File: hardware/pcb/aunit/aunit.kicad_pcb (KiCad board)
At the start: 2 copper layers, 62.2 x 21.6 mm, 48 parts, among them J1 BUS, J2 Input A, J3 Input B, J4 Control, J5 Flags, J6 Power, U1 74HC283, U2 74HC283, U3 74HC86, U4 74HC86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

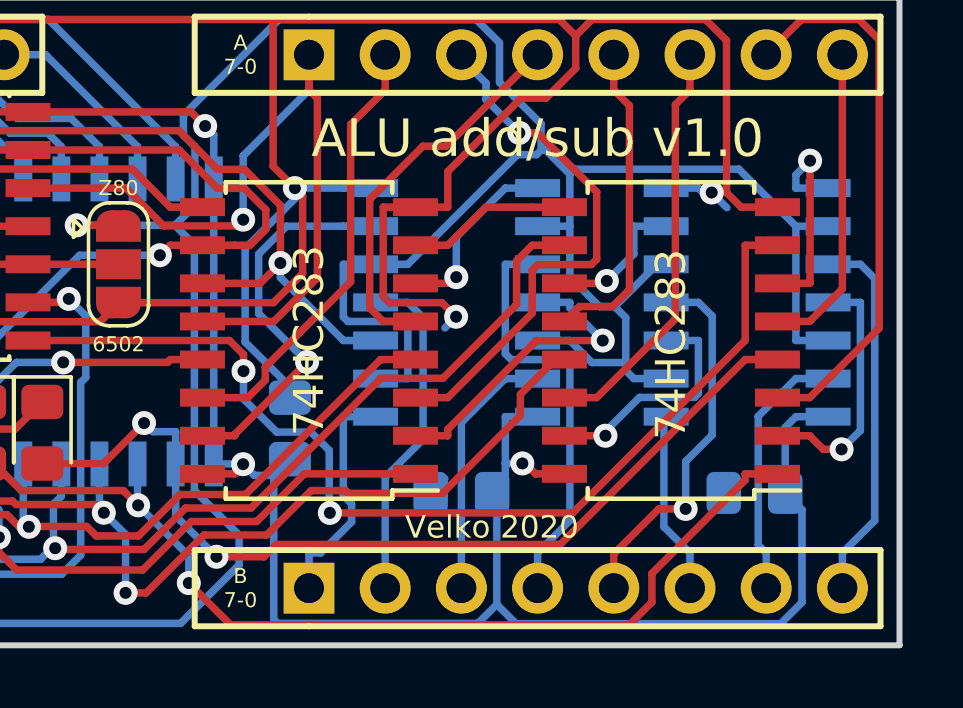
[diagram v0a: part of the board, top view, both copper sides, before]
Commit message: Corrected adder footprints on AUnit, needs re-routing
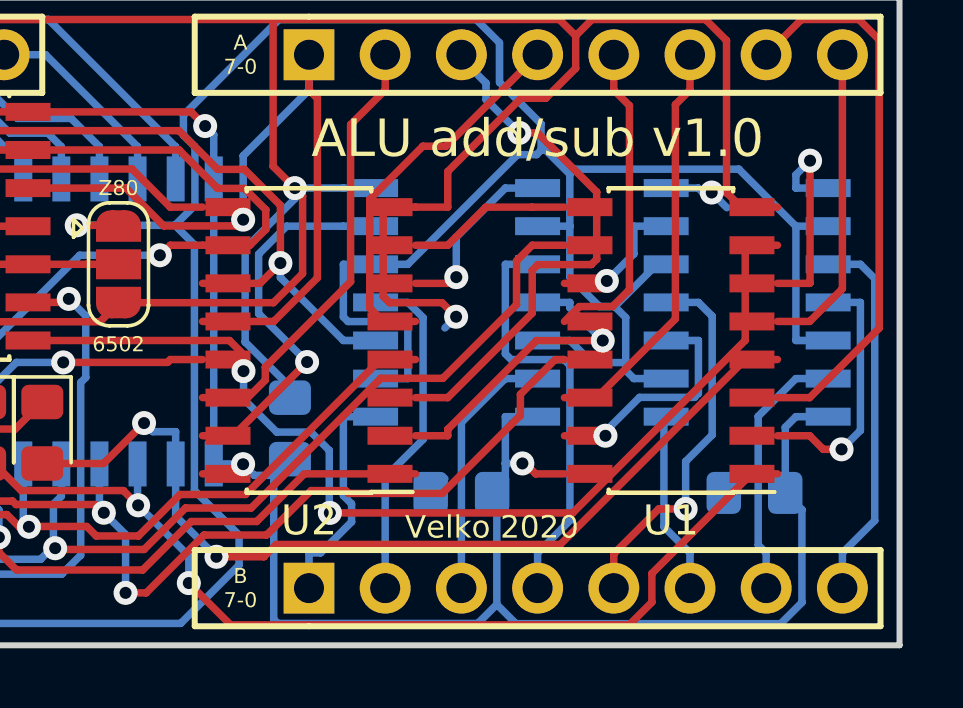
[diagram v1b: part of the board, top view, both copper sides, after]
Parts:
- U1, U2: footprint Package_SO:SOIC-16W_5.3x10.2mm_P1.27mm -> Package_SO:SOIC-16_3.9x9.9mm_P1.27mm

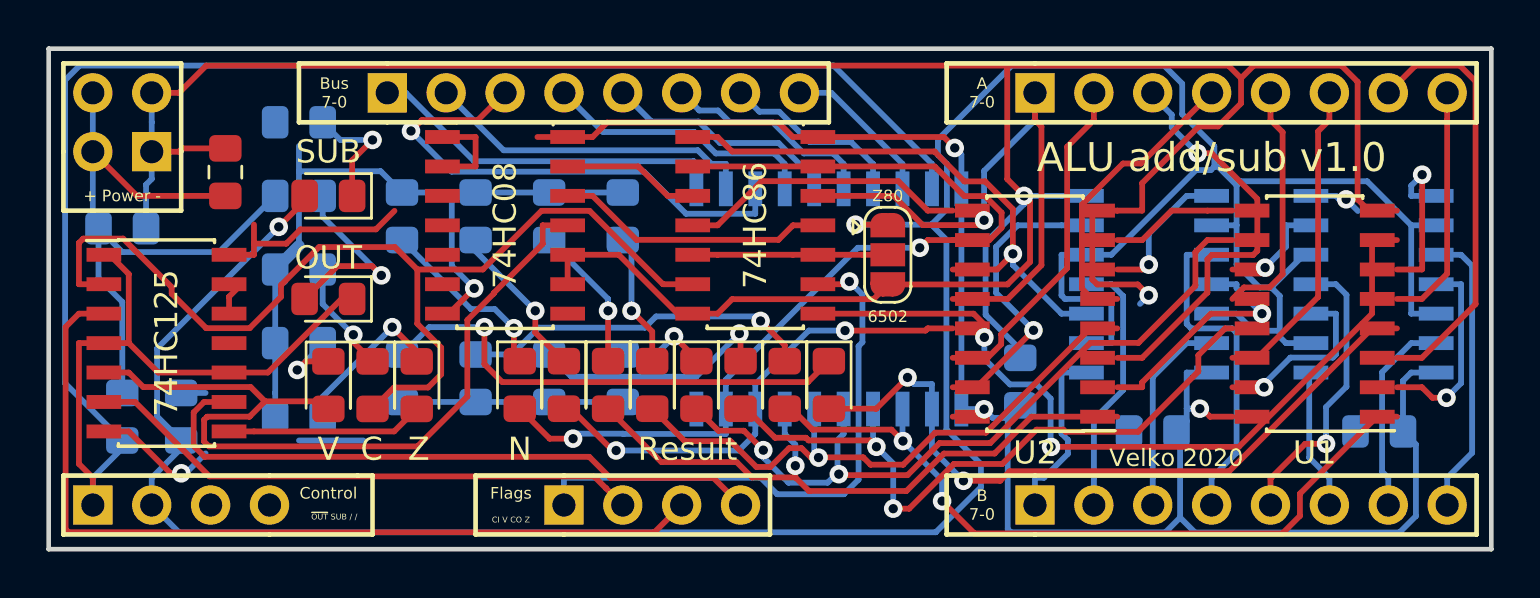
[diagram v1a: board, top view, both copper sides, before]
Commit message: Rerouted for new footprints (checkpoint)
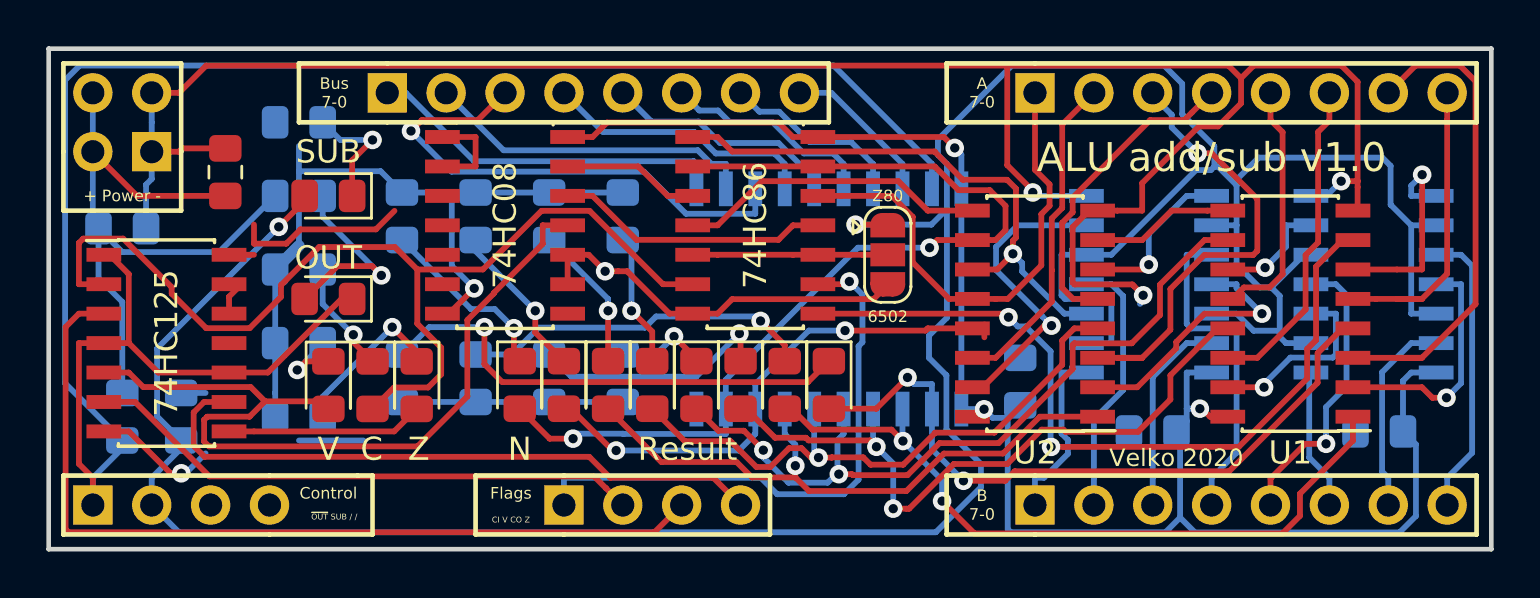
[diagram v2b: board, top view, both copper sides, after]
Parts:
- moved U1 1.05 mm to (88.5, 47.6)
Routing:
- net GND: track 184.0 -> 165.3 mm, vias 5 -> 6
- net A7: track 26.2 -> 21.1 mm, vias 1 -> 0
- net ADD_SUB: track 137.7 -> 140.7 mm
- net A1: track 18.5 -> 21.5 mm
- net A0: track 10.4 -> 13.4 mm
- net VCC: track 119.8 -> 117.0 mm
- net A5: track 17.8 -> 19.9 mm
- net /B1I: track 8.56 -> 10.5 mm
- net /B0I: track 7.36 -> 9.25 mm
- net SUM1: track 33.3 -> 31.9 mm
- net SUM6: track 21.0 -> 22.2 mm
- net SUM0: track 31.3 -> 30.1 mm
- net SUM7: track 41.3 -> 42.4 mm
- net SUM5: track 27.9 -> 26.8 mm
- net /B4I: track 6.17 -> 7.09 mm
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
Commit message: Power and ground plane optimizations
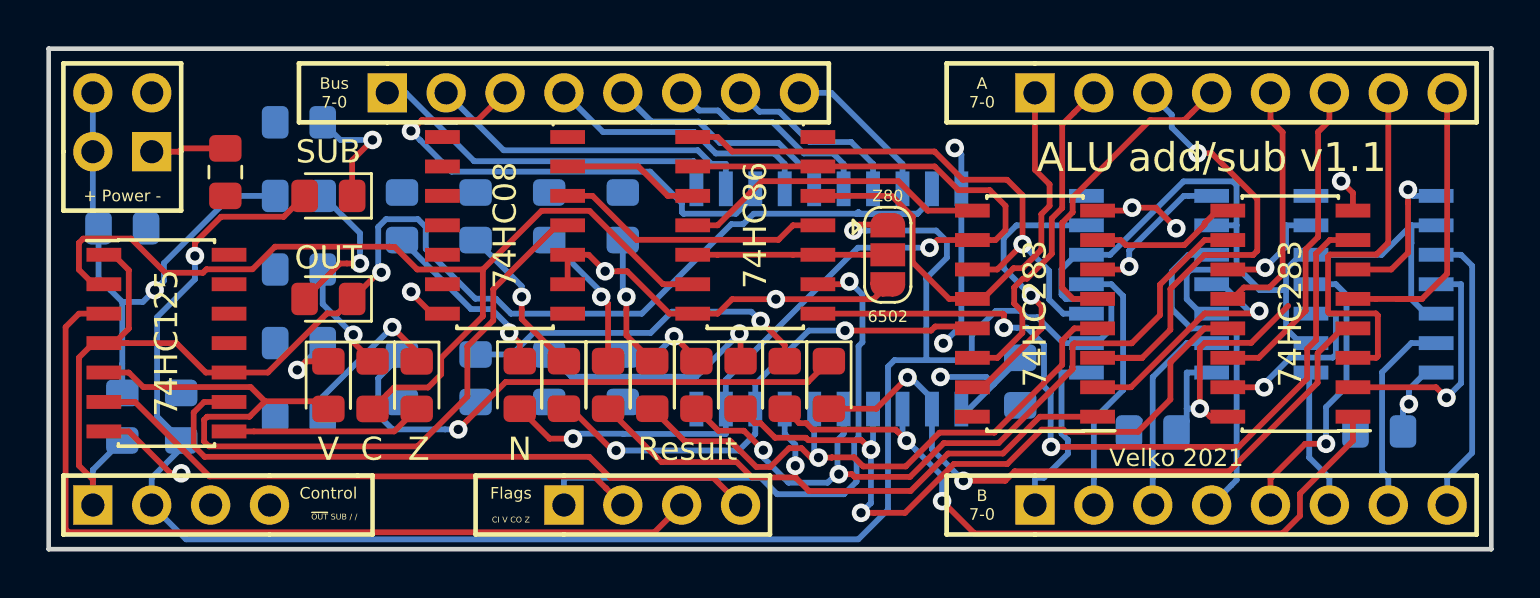
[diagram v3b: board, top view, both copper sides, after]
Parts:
- turned C2 to 270 degrees
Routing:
- net GND: track 165.3 -> 32.3 mm, vias 6 -> 7
- net VCC: track 117.0 -> 55.1 mm, vias 3 -> 6
- net ~OUT~: track 85.6 -> 64.2 mm, vias 0 -> 1
- net ADD_SUB: track 140.7 -> 123.7 mm
- net A1: track 21.5 -> 16.8 mm
- net Net-(D0-Pad1): track 21.2 -> 24.0 mm
- net /B0I: track 9.25 -> 6.76 mm
- net CARRYD: track 44.2 -> 41.7 mm
- net Net-(D8-Pad2): track 8.54 -> 6.60 mm
- net SUM2: track 30.1 -> 31.7 mm
- net /B6I: track 13.2 -> 12.4 mm
- net /CII: track 34.2 -> 34.8 mm
- net B7I: track 24.2 -> 24.7 mm
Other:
- board text added: "ALU add/sub v1.1"
- board text added: "Velko 2021"
- board text removed: "ALU add/sub v1.0"
- board text removed: "Velko 2020"

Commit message: Remove all tracks
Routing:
- net ADD_SUB: track 123.7 -> 0.00 mm, vias 2 -> 0
- net ~OUT~: track 64.2 -> 0.00 mm, vias 1 -> 0
- net VCC: track 55.1 -> 0.00 mm, vias 6 -> 0
- net SUM7: track 42.4 -> 0.00 mm, vias 2 -> 0
- net CARRYD: track 41.7 -> 0.00 mm
- net COUT: track 37.7 -> 0.00 mm
- net OVFD: track 36.0 -> 0.00 mm
- net /CII: track 34.8 -> 0.00 mm, vias 2 -> 0
- net SUM3: track 33.3 -> 0.00 mm, vias 2 -> 0
- net GND: track 32.3 -> 0.00 mm, vias 7 -> 0
- net SUM1: track 32.1 -> 0.00 mm, vias 2 -> 0
- net SUM2: track 31.7 -> 0.00 mm, vias 2 -> 0
- net SUM0: track 29.8 -> 0.00 mm, vias 2 -> 0
- net ZIN: track 27.8 -> 0.00 mm
- net SUM5: track 26.8 -> 0.00 mm, vias 1 -> 0
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- removed copper zone on B.Cu, net GND
- removed copper zone on F.Cu, net VCC

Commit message: Move stuff around
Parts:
- added C6: 100nF, Capacitor_SMD:C_0805_2012Metric_Pad1.15x1.40mm_HandSolder, F.Cu at (59.3, 41.3)
- added C7: 100nF, Capacitor_SMD:C_0805_2012Metric_Pad1.15x1.40mm_HandSolder, F.Cu at (79.2, 53.3)
- added C8: 100nF, Capacitor_SMD:C_0805_2012Metric_Pad1.15x1.40mm_HandSolder, F.Cu at (71.0, 40.4)
- added C9: 100nF, Capacitor_SMD:C_0805_2012Metric_Pad1.15x1.40mm_HandSolder, F.Cu at (90.4, 53.2)
- moved R4 3.81 mm to (56.3, 45.1)
- moved U2 3.72 mm to (81.2, 47.1)
- moved U1 3.50 mm to (91.9, 47.1)
- moved R3 3.43 mm to (56.3, 50.4)
- moved R5 2.82 mm to (54.2, 45.1)
- moved C2 2.80 mm to (74.0, 50.7), turned to 90 degrees
- moved U7 2.29 mm to (66.3, 46.9)
- moved R2 2.29 mm to (54.2, 50.4)
- moved R6 2.01 mm to (52.2, 45.1)
- moved R7 1.65 mm to (50.2, 45.1)
- moved C5 1.49 mm to (93.7, 52.2)
- moved U4 1.28 mm to (81.1, 46.5)
- moved R1 1.14 mm to (52.2, 50.4)
- moved C3 0.81 mm to (42.8, 42.3)
- moved C4 0.63 mm to (82.9, 52.2)
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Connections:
- U4 pad 1: B7 -> B6
- U4 pad 3: B7I -> /B6I
- U4 pad 4: B6 -> B7
- U4 pad 6: /B6I -> B7I
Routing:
- net SUM0: track 0.00 -> 3.30 mm, vias 0 -> 2
- net SUM5: track 0.00 -> 3.29 mm, vias 0 -> 2
- net SUM1: track 0.00 -> 3.28 mm, vias 0 -> 2
- net SUM4: track 0.00 -> 2.92 mm, vias 0 -> 2
- net SUM7: track 0.00 -> 2.87 mm, vias 0 -> 2
- net SUM6: track 0.00 -> 2.85 mm, vias 0 -> 2
- net SUM3: track 0.00 -> 2.85 mm, vias 0 -> 2
- net SUM2: track 0.00 -> 2.85 mm, vias 0 -> 2

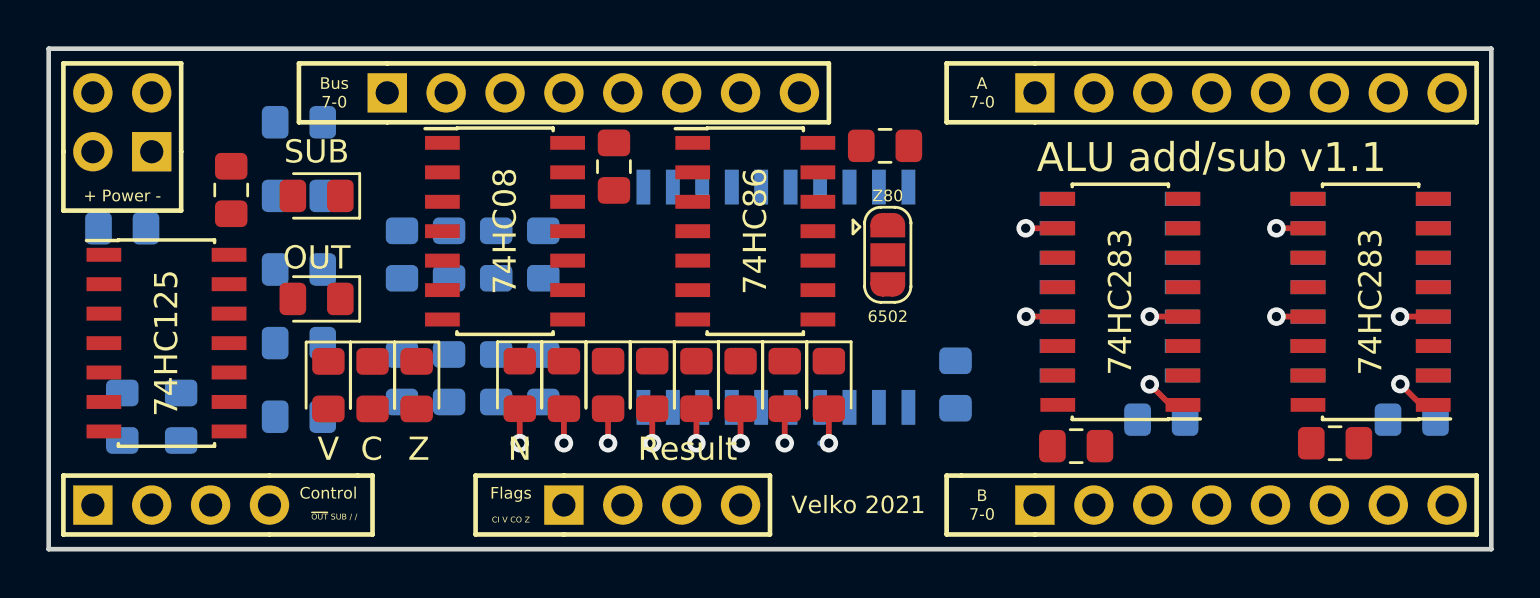
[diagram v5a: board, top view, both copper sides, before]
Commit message: Routed AUnit on 4-layer
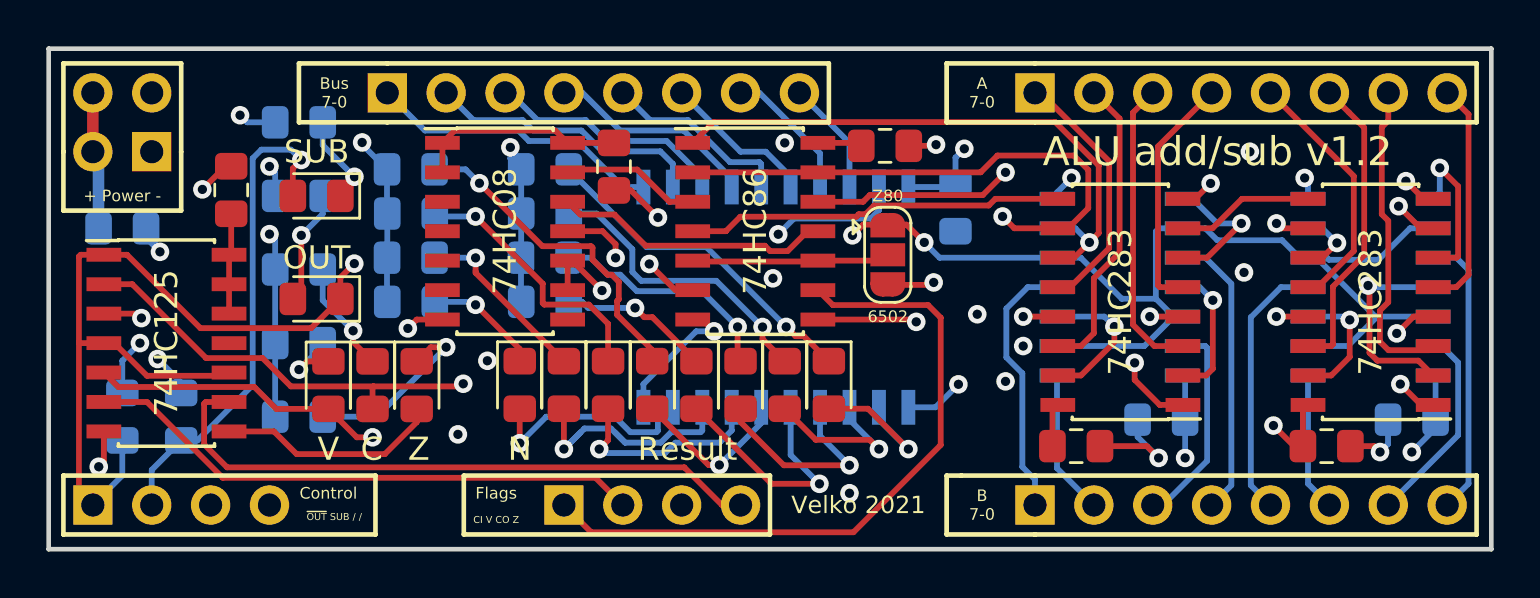
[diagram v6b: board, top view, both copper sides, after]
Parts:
- moved R0 10.9 mm to (56.3, 41.4), turned to 0 degrees
- moved R1 8.22 mm to (56.3, 43.3), turned to 0 degrees
- moved C2 7.64 mm to (74.0, 43.0), turned to 270 degrees
- moved R4 6.79 mm to (50.5, 41.4), turned to 0 degrees
- moved R2 5.60 mm to (56.3, 45.2), turned to 0 degrees
- moved R5 4.08 mm to (50.6, 43.3), turned to 0 degrees
- moved R3 3.29 mm to (56.3, 47.1), turned to 0 degrees
- moved R7 2.08 mm to (50.6, 47.1), turned to 0 degrees
- moved R6 1.66 mm to (50.5, 45.2), turned to 0 degrees
- moved C9 0.38 mm to (90.1, 53.3)
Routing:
- net ADD_SUB: track 0.00 -> 94.0 mm, vias 0 -> 3
- net ~OUT~: track 0.00 -> 60.9 mm, vias 0 -> 2
- net GND: track 0.00 -> 59.7 mm, vias 0 -> 21
- net SUM7: track 2.87 -> 58.2 mm
- net VCC: track 0.00 -> 44.6 mm, vias 0 -> 16
- net SUM3: track 2.85 -> 38.0 mm
- net SUM5: track 3.29 -> 37.1 mm
- net SUM6: track 2.85 -> 36.3 mm
- net CARRYD: track 0.00 -> 31.0 mm, vias 0 -> 2
- net SUM1: track 3.28 -> 33.5 mm
- net CIN: track 0.00 -> 29.6 mm
- net SUM2: track 2.85 -> 32.4 mm
- net OVFD: track 0.00 -> 29.6 mm, vias 0 -> 2
- net /CII: track 0.00 -> 29.0 mm, vias 0 -> 2
- net SUM4: track 2.92 -> 31.5 mm
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- added copper zone on B.Cu, net GND
- added copper zone on In2.Cu, net GND
- added copper zone on F.Cu, net VCC
- added copper zone on In1.Cu, net VCC
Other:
- copper layers 2 -> 4
- board text added: "ALU add/sub v1.2"
- board text added: "JLCJLCJLCJLC"
- board text removed: "ALU add/sub v1.1"
